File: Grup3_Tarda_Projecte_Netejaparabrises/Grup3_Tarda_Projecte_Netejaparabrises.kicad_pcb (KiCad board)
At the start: 2 copper layers, 0 parts

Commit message: Layout 3
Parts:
- added C1: 100n, Capacitor_SMD:C_0805_2012Metric, F.Cu at (38.5, 68.0)
- added C2: 0.33u, Capacitor_THT:C_Disc_D3.0mm_W1.6mm_P2.50mm, F.Cu at (37.8, 65.2)
- added C3: 0.1u, Capacitor_THT:C_Disc_D3.0mm_W1.6mm_P2.50mm, F.Cu at (37.8, 44.6)
- added C4: 100n, Capacitor_SMD:C_0805_2012Metric, F.Cu at (38.5, 42.1)
- added CClock1: 22p, Capacitor_SMD:C_0805_2012Metric, F.Cu at (105.3, 61.2)
- added CClock2: 22p, Capacitor_SMD:C_0805_2012Metric, F.Cu at (105.3, 73.4)
- added CDesOpam1: 100n, Capacitor_SMD:C_0805_2012Metric, F.Cu at (77.0, 67.2)
- added CDesacobCan1: 100n, Capacitor_SMD:C_0805_2012Metric, F.Cu at (138.8, 72.6)
- added CDesacobMicro1: 100n, Capacitor_SMD:C_0805_2012Metric, F.Cu at (122.6, 66.7)
- added D1: 1N4002, Diode_THT:D_DO-41_SOD81_P10.16mm_Horizontal, F.Cu at (38.4, 75.6)
- added D10: 1N5400, Diode_THT:D_DO-201AD_P15.24mm_Horizontal, F.Cu at (161.8, 91.9)
- added D11: 1N5400, Diode_THT:D_DO-201AD_P15.24mm_Horizontal, F.Cu at (193.3, 92.0)
- added D12: 1N5400, Diode_THT:D_DO-201AD_P15.24mm_Horizontal, F.Cu at (221.2, 118.0)
- added D2: 35V, Diode_THT:D_5W_P5.08mm_Vertical_AnodeUp, F.Cu at (38.9, 71.8)
- added D3: LED, LED_SMD:LED_0805_2012Metric_Pad1.15x1.40mm_HandSolder, F.Cu at (38.7, 49.7)
- added D4: 1N5400, Diode_THT:D_DO-201AD_P15.24mm_Horizontal, F.Cu at (221.2, 87.4)
- added D5: 1N5400, Diode_THT:D_DO-201AD_P15.24mm_Horizontal, F.Cu at (43.3, 92.2)
- added D6: 1N5400, Diode_THT:D_DO-201AD_P15.24mm_Horizontal, F.Cu at (102.2, 91.8)
- added D7: 1N5400, Diode_THT:D_DO-201AD_P15.24mm_Horizontal, F.Cu at (72.3, 92.0)
- added D8: 1N5400, Diode_THT:D_DO-201AD_P15.24mm_Horizontal, F.Cu at (221.2, 46.5)
- added D9: 1N5400, Diode_THT:D_DO-201AD_P15.24mm_Horizontal, F.Cu at (131.8, 92.1)
- added FL1: BLM03HD331SZ1D, BLM03HD331SZ1D:BEADC0603X33N, F.Cu at (47.8, 57.3)
- added FL2: BLM03HD331SZ1D, BLM03HD331SZ1D:BEADC0603X33N, F.Cu at (86.0, 83.0)
- added FL3: BLM03HD331SZ1D, BLM03HD331SZ1D:BEADC0603X33N, F.Cu at (162.0, 83.0)
- added FL4: BLM03HD331SZ1D, BLM03HD331SZ1D:BEADC0603X33N, F.Cu at (213.2, 73.1)
- added IC1: L78S05CV, L78S05CV:TO-220-STANDING, F.Cu at (39.8, 57.3)
- added IC2: PIC18F258-I_SO, Package_SO:SOIC-28W_7.5x17.9mm_P1.27mm, F.Cu at (114.8, 64.8)
- added J1: Screw_Terminal_01x02, Connector_PinSocket_2.54mm:PinSocket_1x02_P2.54mm_Vertical, F.Cu at (34.1, 91.0)
- added J2: BOTONERA, Connector_PinSocket_2.54mm:PinSocket_1x06_P2.54mm_Vertical, F.Cu at (102.5, 31.3)
- added J3: PROGRAMMING CON, Connector_PinSocket_2.54mm:PinSocket_1x05_P2.54mm_Vertical, F.Cu at (143.5, 52.2)
- added J4: JP1, Connector_PinSocket_2.54mm:PinSocket_1x03_P2.54mm_Vertical, F.Cu at (131.4, 56.5)
- added J5: DE9_Plug_MountingHoles, Connector_Dsub:DSUB-9_Female_Horizontal_P2.77x2.84mm_EdgePinOffset4.94mm_Housed_MountingHolesOffset7.48mm, F.Cu at (158.9, 43.7)
- added J6: DE9_Plug_MountingHoles, Connector_Dsub:DSUB-9_Female_Horizontal_P2.77x2.84mm_EdgePinOffset4.94mm_Housed_MountingHolesOffset7.48mm, F.Cu at (191.5, 43.7)
- added J7: CONEXIOSENSOR, Connector_PinSocket_2.54mm:PinSocket_1x02_P2.54mm_Vertical, F.Cu at (68.0, 54.6)
- added J8: CONNECTOR ALIMENTACIO 01x10, Connector_PinSocket_2.54mm:PinSocket_1x10_P2.54mm_Vertical, F.Cu at (184.9, 124.8)
- added K1: 1393280-6, V23076A1001C133:V23076A1001C133, F.Cu at (233.9, 87.4)
- added K2: 1393280-6, V23076A1001C133:V23076A1001C133, F.Cu at (34.4, 104.6)
- added K3: 1393280-6, V23076A1001C133:V23076A1001C133, F.Cu at (93.2, 104.6)
- added K4: 1393280-6, V23076A1001C133:V23076A1001C133, F.Cu at (63.3, 104.7)
- added K5: 1393280-6, V23076A1001C133:V23076A1001C133, F.Cu at (234.1, 55.3)
- added K6: 1393280-6, V23076A1001C133:V23076A1001C133, F.Cu at (122.9, 104.7)
- added K7: 1393280-6, V23076A1001C133:V23076A1001C133, F.Cu at (152.8, 104.7)
- added K8: 1393280-6, V23076A1001C133:V23076A1001C133, F.Cu at (184.2, 104.6)
- added K9: 1393280-6, V23076A1001C133:V23076A1001C133, F.Cu at (233.8, 117.9)
- added Q1: BC817-25_RF, BC817-25_RF:SOT95P237X112-3N, F.Cu at (219.9, 67.2)
- added Q2: BC817-25_RF, BC817-25_RF:SOT95P237X112-3N, F.Cu at (127.8, 92.9)
- added Q3: BC817-25_RF, BC817-25_RF:SOT95P237X112-3N, F.Cu at (98.2, 92.7)
- added Q4: BC817-25_RF, BC817-25_RF:SOT95P237X112-3N, F.Cu at (219.6, 52.0)
- added Q5: BC817-25_RF, BC817-25_RF:SOT95P237X112-3N, F.Cu at (157.8, 92.8)
- added Q6: BC817-25_RF, BC817-25_RF:SOT95P237X112-3N, F.Cu at (189.2, 92.9)
- added Q7: BC817-25_RF, BC817-25_RF:SOT95P237X112-3N, F.Cu at (222.2, 93.5)
- added R1: 220, Resistor_SMD:R_0805_2012Metric_Pad1.20x1.40mm_HandSolder, F.Cu at (38.6, 47.1)
- added R10: 13.4R, Resistor_SMD:R_0805_2012Metric_Pad1.20x1.40mm_HandSolder, F.Cu at (95.2, 92.6)
- added R11: 620.3R, Resistor_SMD:R_0805_2012Metric_Pad1.20x1.40mm_HandSolder, F.Cu at (216.4, 57.0)
- added R12: 319.6R, Resistor_SMD:R_0805_2012Metric_Pad1.20x1.40mm_HandSolder, F.Cu at (219.3, 57.0)
- added R13: 13.4R, Resistor_SMD:R_0805_2012Metric_Pad1.20x1.40mm_HandSolder, F.Cu at (222.3, 57.0)
- added R14: 620.3R, Resistor_SMD:R_0805_2012Metric_Pad1.20x1.40mm_HandSolder, F.Cu at (155.6, 87.5)
- added R15: 620.3R, Resistor_SMD:R_0805_2012Metric_Pad1.20x1.40mm_HandSolder, F.Cu at (186.9, 87.5)
- added R16: 319.6R, Resistor_SMD:R_0805_2012Metric_Pad1.20x1.40mm_HandSolder, F.Cu at (155.6, 89.6)
- added R17: 319.6R, Resistor_SMD:R_0805_2012Metric_Pad1.20x1.40mm_HandSolder, F.Cu at (186.9, 89.8)
- added R18: 13.4R, Resistor_SMD:R_0805_2012Metric_Pad1.20x1.40mm_HandSolder, F.Cu at (154.7, 92.9)
- added R19: 13.4R, Resistor_SMD:R_0805_2012Metric_Pad1.20x1.40mm_HandSolder, F.Cu at (186.1, 93.0)
- added R2: 620.3R, Resistor_SMD:R_0805_2012Metric_Pad1.20x1.40mm_HandSolder, F.Cu at (216.9, 62.7)
- added R20: 620.3R, Resistor_SMD:R_0805_2012Metric_Pad1.20x1.40mm_HandSolder, F.Cu at (216.4, 96.0)
- added R21: 319.6R, Resistor_SMD:R_0805_2012Metric_Pad1.20x1.40mm_HandSolder, F.Cu at (218.8, 96.0)
- added R22: 13.4R, Resistor_SMD:R_0805_2012Metric_Pad1.20x1.40mm_HandSolder, F.Cu at (222.1, 96.9)
- added R3: 620.3R, Resistor_SMD:R_0805_2012Metric_Pad1.20x1.40mm_HandSolder, F.Cu at (125.4, 87.3)
- added R4: 620.3R, Resistor_SMD:R_0805_2012Metric_Pad1.20x1.40mm_HandSolder, F.Cu at (96.2, 87.2)
- added R5: 319.6R, Resistor_SMD:R_0805_2012Metric_Pad1.20x1.40mm_HandSolder, F.Cu at (220.1, 62.7)
- added R6: 319.6R, Resistor_SMD:R_0805_2012Metric_Pad1.20x1.40mm_HandSolder, F.Cu at (125.5, 89.7)
- added R7: 319.6R, Resistor_SMD:R_0805_2012Metric_Pad1.20x1.40mm_HandSolder, F.Cu at (96.2, 89.5)
- added R8: 13.4R, Resistor_SMD:R_0805_2012Metric_Pad1.20x1.40mm_HandSolder, F.Cu at (223.1, 62.7)
- added R9: 13.4R, Resistor_SMD:R_0805_2012Metric_Pad1.20x1.40mm_HandSolder, F.Cu at (124.7, 92.9)
- added RBot1: 22k, Resistor_SMD:R_0805_2012Metric_Pad1.20x1.40mm_HandSolder, F.Cu at (102.9, 50.4)
- added RBot2: 22k, Resistor_SMD:R_0805_2012Metric_Pad1.20x1.40mm_HandSolder, F.Cu at (105.7, 50.4)
- added RBot3: 22k, Resistor_SMD:R_0805_2012Metric_Pad1.20x1.40mm_HandSolder, F.Cu at (109.0, 50.4)
- added RBot4: 22k, Resistor_SMD:R_0805_2012Metric_Pad1.20x1.40mm_HandSolder, F.Cu at (112.4, 50.4)
- added RPOT1: 10k, POTENCIOMETRE:TRIM_3362P-1-103, F.Cu at (68.5, 61.4)
- added RReset1: 4.7k, Resistor_SMD:R_0805_2012Metric_Pad1.20x1.40mm_HandSolder, F.Cu at (134.2, 60.0)
- added RSens1: 1k, Resistor_SMD:R_0805_2012Metric_Pad1.20x1.40mm_HandSolder, F.Cu at (74.5, 56.6)
- added Rterm1: 120R, Resistor_SMD:R_0805_2012Metric_Pad1.20x1.40mm_HandSolder, F.Cu at (149.3, 71.8)
- added SW1: SW_SPST, Library:AS11CH, F.Cu at (109.0, 40.3)
- added SW2: SW_SP3T, SW_NR01103ANG13-1C:SW_NR01103ANG13-1C, F.Cu at (120.6, 41.7)
- added SWReset1: SW_Push, Button_Switch_SMD:SW_Push_SPST_NO_Alps_SKRK, F.Cu at (136.0, 56.4)
- added U1: Value, Package_SO:SOIC-8_3.9x4.9mm_P1.27mm, F.Cu at (144.3, 71.8)
- added U2: LM393, Package_SO:SOIC-8_3.9x4.9mm_P1.27mm, F.Cu at (75.3, 61.5)
- added Y1: ABLS2-8.000MHZ-D4Y-T, XTAL_ABLS2-8:XTAL_ABLS2-8.000MHZ-D4Y-T, F.Cu at (101.5, 67.3)
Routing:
- net DriverM2: track 0.00 -> 149.6 mm
- net VMOT1-: track 0.00 -> 123.8 mm
- net VBOMBA2: track 0.00 -> 110.4 mm
- net DriverB1: track 0.00 -> 99.0 mm, vias 0 -> 2
- net VMOT1+: track 0.00 -> 90.5 mm
- net VBOMBA1: track 0.00 -> 75.8 mm
- net /Digital/Tx: track 0.00 -> 68.8 mm
- net /Digital/Rx: track 0.00 -> 66.8 mm
- net EN2: track 0.00 -> 66.7 mm
- net EN1: track 0.00 -> 65.4 mm
- net /Potencia/Vc_m2: track 0.00 -> 62.8 mm
- net /Digital/CANH: track 0.00 -> 61.8 mm
- net /Potencia/Vc_m1: track 0.00 -> 61.4 mm
- net /Digital/CANL: track 0.00 -> 59.7 mm
- net VLUNETA: track 0.00 -> 45.4 mm
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- added copper zone on In1.Cu, net +VCC
- added copper zone on F.Cu, net GND
- added copper zone on In2.Cu, net GND
- added copper zone on In2.Cu, net GNDPWR
- added copper zone on In1.Cu, net VBAT
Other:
- board outline added: 254.4 x 101.6 mm
- copper layers 2 -> 4

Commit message: canvis divisor sensor de pluja, node vbat protegit, connector de motors, README
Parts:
- moved FL2 125.6 mm to (148.0, -26.3)
- moved K9 118.2 mm to (118.0, 141.6), turned to 0 degrees
- moved FL3 116.8 mm to (190.8, -30.1)
- moved D12 103.9 mm to (117.8, 129.1), turned to 0 degrees
- moved FL4 103.7 mm to (228.5, -29.4)
- moved FL1 103.5 mm to (113.8, -22.5)
- moved K5 101.9 mm to (180.6, 142.0), turned to 0 degrees
- moved K1 101.2 mm to (148.5, 141.8), turned to 0 degrees
- moved R22 89.5 mm to (139.0, 130.0), turned to 90 degrees
- moved J8 88.9 mm to (258.0, 74.1), turned to 0 degrees
- moved D8 88.6 mm to (189.4, 129.1), turned to 0 degrees
- moved Q7 87.7 mm to (142.4, 130.0), turned to -90 degrees
- moved R13 85.1 mm to (178.9, 130.2), turned to 0 degrees
- moved R21 84.6 mm to (139.9, 126.7), turned to 0 degrees
- moved R8 84.6 mm to (173.2, 131.0), turned to 0 degrees
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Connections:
- C1 pad 1: /Alimentacio/V_{in} -> VBAT
- C2 pad 1: /Alimentacio/V_{in} -> VBAT
- C3 pad 2: GNDPWR -> GND
- C4 pad 2: GNDPWR -> GND
- D1 pad 1: /Alimentacio/V_{in} -> VBAT
- D1 pad 2: VBAT -> /Alimentacio/Vbat
- D2 pad 1: /Alimentacio/V_{in} -> VBAT
- IC1 pad 1: /Alimentacio/V_{in} -> VBAT
- J1 pad 1: VBAT -> /Alimentacio/Vbat
- R1 pad 2: GNDPWR -> GND
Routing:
- net DriverM2: track 149.6 -> 0.00 mm
- net VMOT1-: track 123.8 -> 0.00 mm
- net VBOMBA2: track 110.4 -> 0.00 mm
- net DriverB1: track 99.0 -> 0.00 mm, vias 2 -> 0
- net VMOT1+: track 90.5 -> 0.00 mm
- net VBOMBA1: track 75.8 -> 0.00 mm
- net /Digital/Tx: track 68.8 -> 0.00 mm
- net /Digital/Rx: track 66.8 -> 0.00 mm
- net EN2: track 66.7 -> 0.00 mm
- net EN1: track 65.4 -> 0.00 mm
- net /Potencia/Vc_m2: track 62.8 -> 0.00 mm
- net /Digital/CANH: track 61.8 -> 0.00 mm
- net /Potencia/Vc_m1: track 61.4 -> 0.00 mm
- net /Digital/CANL: track 59.7 -> 0.00 mm
- net VLUNETA: track 45.4 -> 0.00 mm
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- removed copper zone on In1.Cu, net +VCC
- removed copper zone on In2.Cu, net GND
- removed copper zone on In2.Cu, net GNDPWR
- removed copper zone on In1.Cu, net VBAT
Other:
- board outline removed

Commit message: placement
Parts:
- added J10: Screw_Terminal_01x02, TerminalBlock_Phoenix:TerminalBlock_Phoenix_MKDS-1,5-2-5.08_1x02_P5.08mm_Horizontal, F.Cu at (26.2, 109.0)
- added J11: Screw_Terminal_01x02, TerminalBlock_Phoenix:TerminalBlock_Phoenix_MKDS-1,5-2-5.08_1x02_P5.08mm_Horizontal, F.Cu at (169.8, 114.7)
- added J12: Screw_Terminal_01x02, TerminalBlock_Phoenix:TerminalBlock_Phoenix_MKDS-1,5-2-5.08_1x02_P5.08mm_Horizontal, F.Cu at (156.0, 169.2)
- added J9: Screw_Terminal_01x02, TerminalBlock_Phoenix:TerminalBlock_Phoenix_MKDS-1,5-2-5.08_1x02_P5.08mm_Horizontal, F.Cu at (112.0, 169.1)
- added R23: 10k, Resistor_SMD:R_0805_2012Metric_Pad1.20x1.40mm_HandSolder, F.Cu at (53.5, 67.7)
- J1: footprint Connector_PinSocket_2.54mm:PinSocket_1x02_P2.54mm_Vertical -> TerminalBlock_Phoenix:TerminalBlock_Phoenix_MKDS-1,5-2-5.08_1x02_P5.08mm_Horizontal
- J8: value CONNECTOR ALIMENTACIO 01x10 -> Screw_Terminal_01x02; footprint Connector_PinSocket_2.54mm:PinSocket_1x10_P2.54mm_Vertical -> TerminalBlock_Phoenix:TerminalBlock_Phoenix_MKDS-1,5-2-5.08_1x02_P5.08mm_Horizontal
- moved J8 228.6 mm to (49.9, 168.7)
- moved R8 142.8 mm to (34.5, 96.5), turned to 90 degrees
- moved R5 141.9 mm to (35.5, 93.5)
- moved R2 141.6 mm to (35.5, 91.5), turned to 0 degrees
- moved Q1 135.0 mm to (37.4, 96.5), turned to -90 degrees
- moved K1 118.4 mm to (35.0, 108.0)
- moved D4 96.2 mm to (58.2, 95.7), turned to 180 degrees
- moved J5 85.9 mm to (74.1, 57.7)
- moved FL1 79.3 mm to (160.7, 41.5)
- moved Q6 78.5 mm to (122.6, 134.7)
- moved R19 78.5 mm to (119.5, 134.7)
- moved D11 78.5 mm to (126.7, 133.8)
- moved K8 78.5 mm to (117.7, 146.3)
- moved R15 78.5 mm to (120.4, 129.2)
- moved R17 78.5 mm to (120.4, 131.5)
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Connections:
- J8 pad 1: VMOT1+ -> VMOT1-
- J8 pad 2: VMOT1- -> VMOT1+
- RPOT1 pad 1: +VCC -> /Analog/Vsensibilitat
- RPOT1 pad 2: /Analog/Vsensibilitat -> GND
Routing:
- removed copper zone on F.Cu, net GND
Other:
- board outline added: 159.2 x 126.4 mm

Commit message: powersilkscreen
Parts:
- moved J8 6.83 mm to (43.0, 168.9)
- moved RBot1 5.30 mm to (144.4, 83.3)
- moved RBot2 5.30 mm to (144.4, 80.5)
- moved RBot3 5.30 mm to (144.4, 77.2)
- moved RBot4 5.30 mm to (144.4, 73.8)
- moved SW1 5.30 mm to (154.3, 72.3)
- moved SW2 5.30 mm to (166.7, 72.2)
- moved R20 5.19 mm to (174.3, 129.3)
- moved Q7 5.18 mm to (176.8, 135.0)
- moved R21 5.18 mm to (174.3, 131.6)
- moved R22 5.18 mm to (173.4, 135.0)
- moved J12 5.01 mm to (151.0, 168.8)
- moved CDesOpam1 4.86 mm to (52.9, 67.0)
- moved J7 4.86 mm to (43.8, 51.6)
- moved R23 4.86 mm to (48.6, 67.7)
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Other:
- board size 159.2 x 126.4 mm -> 162.4 x 126.4 mm

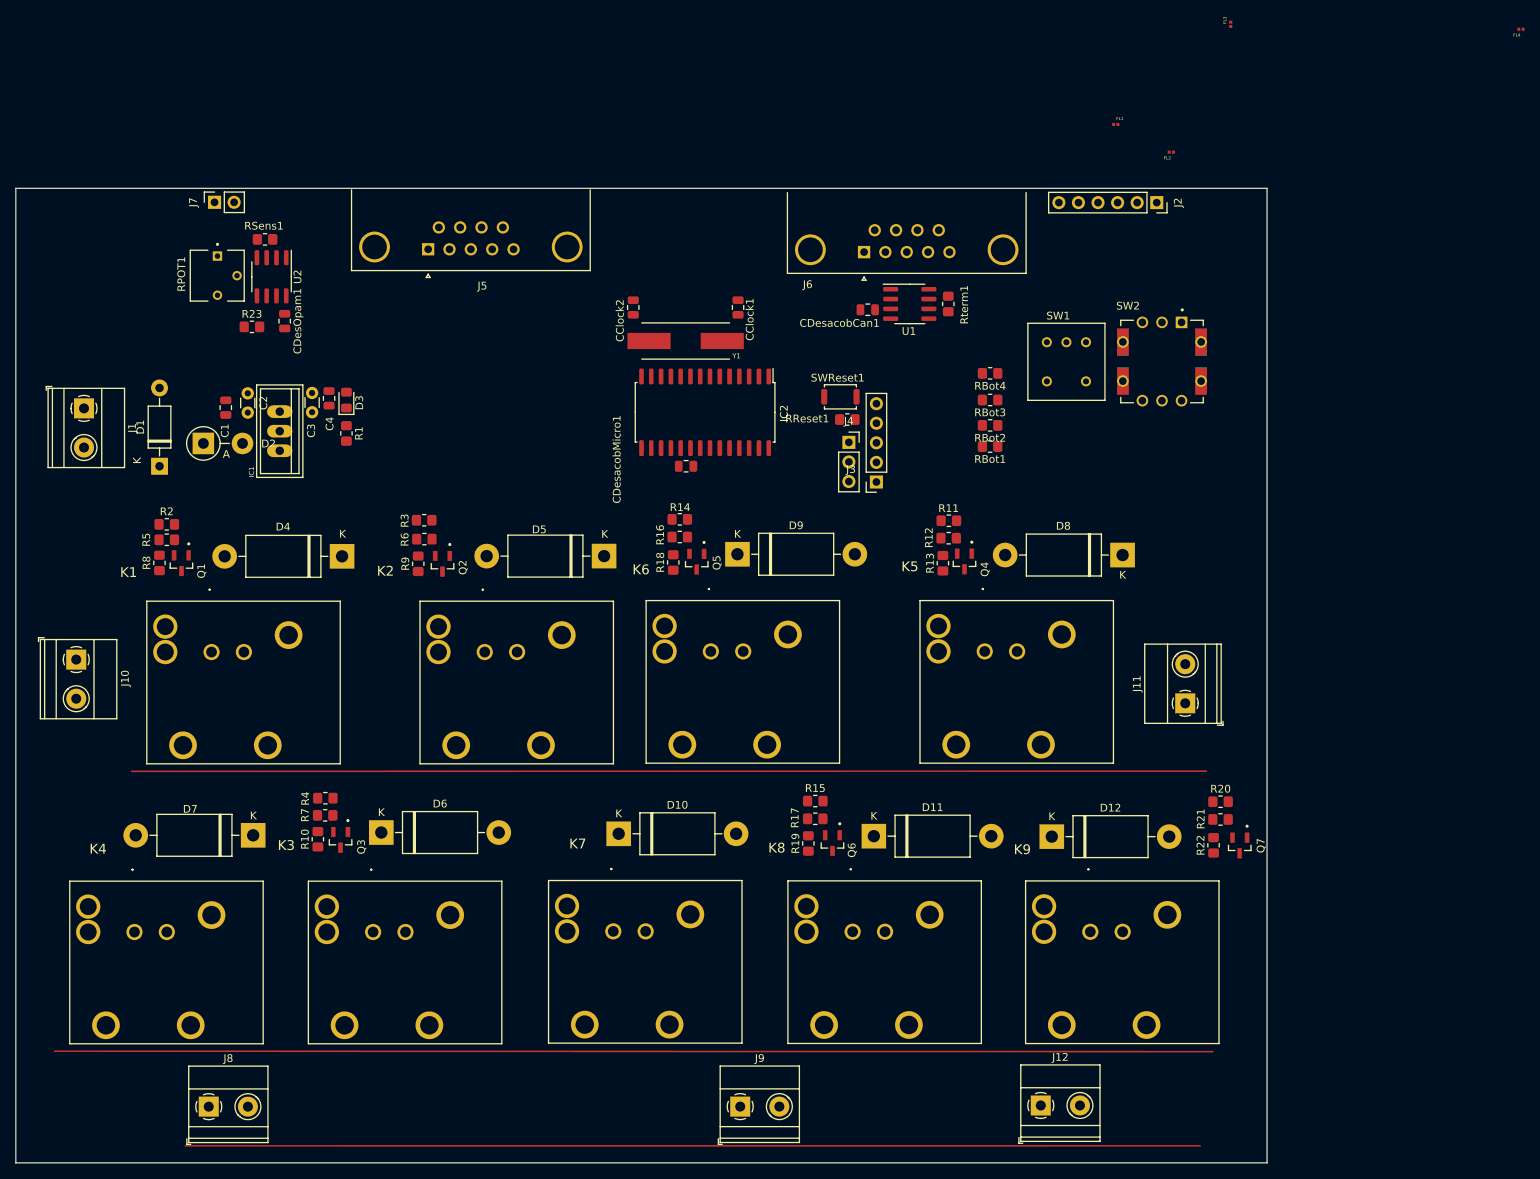
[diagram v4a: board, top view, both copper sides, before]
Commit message: plans de massa i alimentacio layout
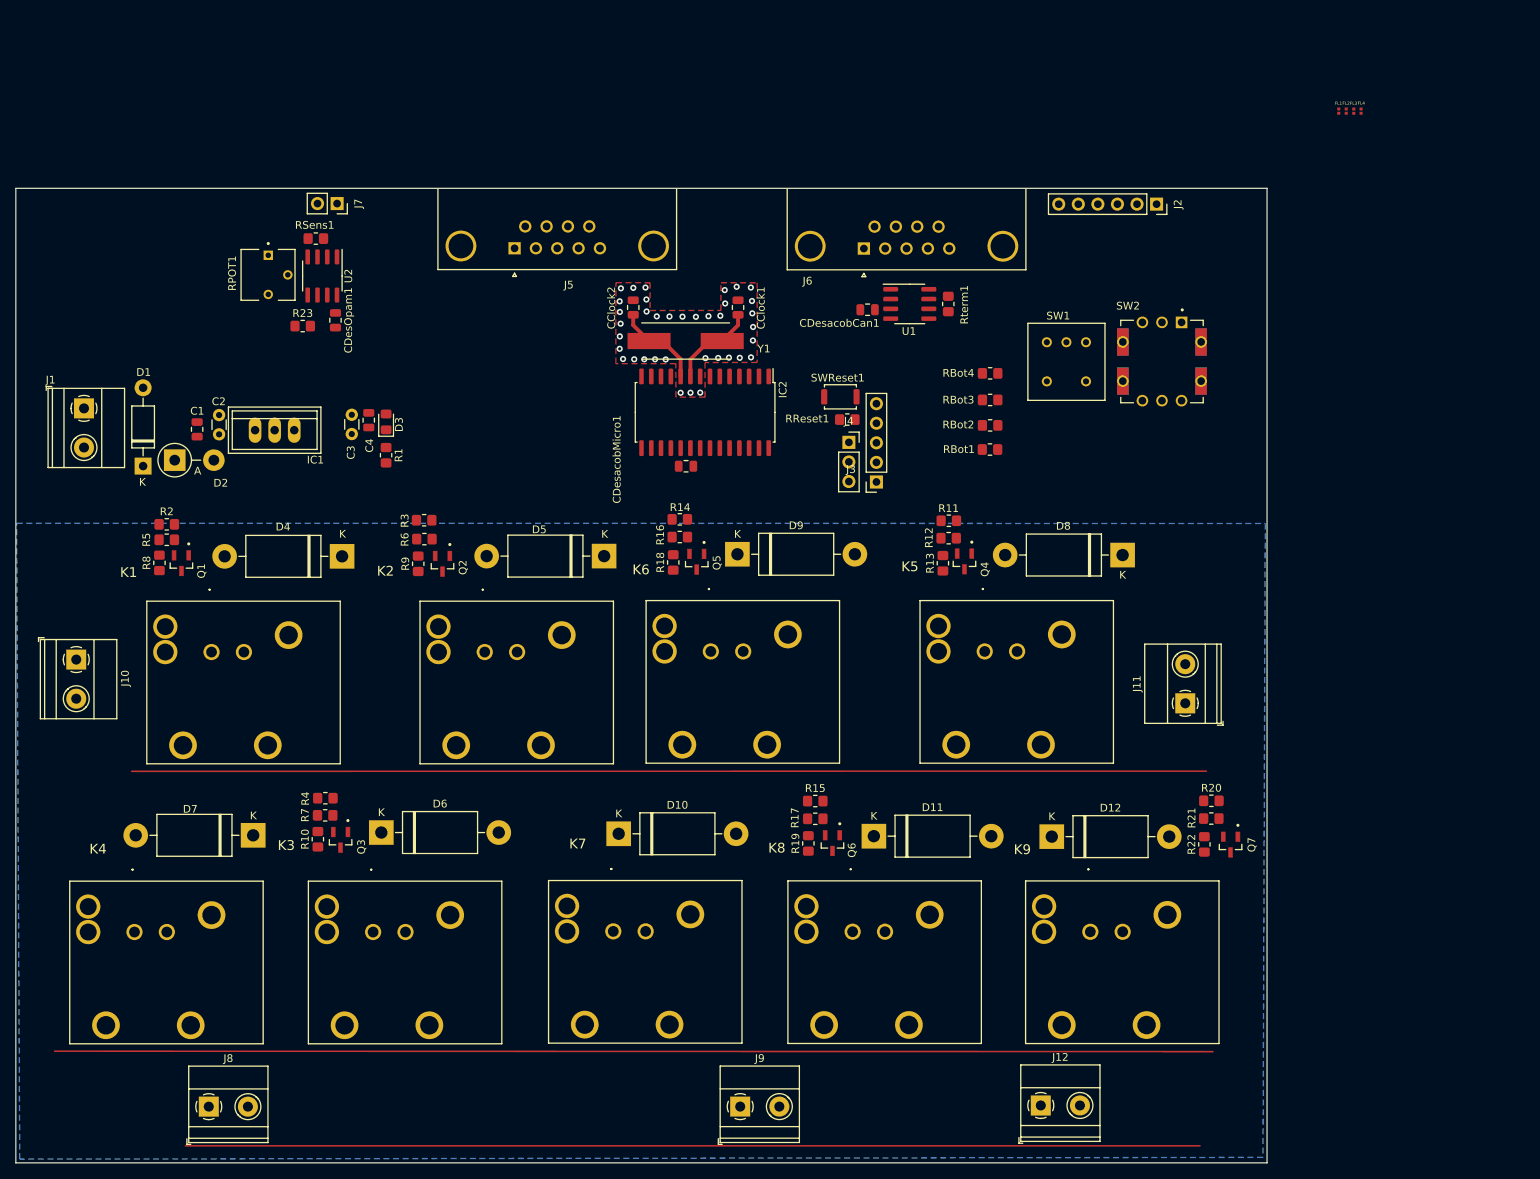
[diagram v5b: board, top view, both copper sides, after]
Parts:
- moved FL1 29.0 mm to (189.7, 39.7), turned to 90 degrees
- moved FL2 23.3 mm to (190.6, 39.7), turned to 90 degrees
- moved FL4 23.3 mm to (192.6, 39.7), turned to 90 degrees
- moved FL3 19.5 mm to (191.6, 39.7)
- moved J7 15.9 mm to (59.7, 51.7), turned to -90 degrees
- moved J5 11.2 mm to (82.7, 57.5)
- moved U2 6.59 mm to (57.8, 61.1)
- moved CDesOpam1 6.59 mm to (59.5, 66.9)
- moved R23 6.59 mm to (55.2, 67.6)
- moved RPOT1 6.59 mm to (50.8, 61.0)
- moved RSens1 6.59 mm to (56.9, 56.3)
- moved D3 5.88 mm to (66.0, 80.1)
- moved C3 5.88 mm to (61.6, 79.1)
- moved C4 5.88 mm to (63.8, 79.8)
- moved R1 5.88 mm to (66.0, 84.4)
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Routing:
- net /Digital/XTAL1: track 0.00 -> 11.6 mm
- net /Digital/XTAL2: track 0.00 -> 11.6 mm
- net GND: vias 0 -> 37
- added copper zone on In1.Cu, net +VCC
- added copper zone on F.Cu, net GND
- added copper zone on In2.Cu, net GND
- added copper zone on B.Cu, net GNDPWR
- added copper zone on In2.Cu, net GNDPWR
- added copper zone on In1.Cu, net VBAT

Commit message: routing v1 sense acabar
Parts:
- removed D2: 35V, Diode_THT:D_5W_P5.08mm_Vertical_AnodeUp
- removed FL1, FL2, FL3, FL4: BLM03HD331SZ1D, BLM03HD331SZ1D:BEADC0603X33N
- removed SW1: SW_SPST, Library:AS11CH
- removed SW2: SW_SP3T, SW_NR01103ANG13-1C:SW_NR01103ANG13-1C
- added REF96: MountingHole_3.2mm_M3_ISO7380, MountingHole:MountingHole_3.2mm_M3_ISO7380, F.Cu at (220.0, 36.8)
- added REF97: MountingHole_3.2mm_M3_ISO7380, MountingHole:MountingHole_3.2mm_M3_ISO7380, F.Cu at (219.8, 155.1)
- added REF98: MountingHole_3.2mm_M3_ISO7380, MountingHole:MountingHole_3.2mm_M3_ISO7380, F.Cu at (65.8, 155.1)
- added REF99: MountingHole_3.2mm_M3_ISO7380, MountingHole:MountingHole_3.2mm_M3_ISO7380, F.Cu at (65.6, 36.7)
- C1, C4, CClock1, CClock2, CDesOpam1, CDesacobCan1, CDesacobMicro1: footprint Capacitor_SMD:C_0805_2012Metric -> Capacitor_THT:C_Disc_D3.0mm_W1.6mm_P2.50mm
- moved D8 51.0 mm to (209.7, 80.3)
- moved D1 49.1 mm to (80.6, 68.8)
- moved Q7 48.8 mm to (221.4, 117.9)
- moved Q4 48.3 mm to (186.3, 81.2)
- moved D3 48.2 mm to (111.2, 63.1)
- moved R1 48.2 mm to (111.2, 67.4)
- moved Q2 48.2 mm to (118.5, 81.5)
- moved Q6 48.0 mm to (168.8, 117.5)
- moved R20 47.7 mm to (216.8, 109.9)
- moved R2 47.6 mm to (81.2, 74.3)
- moved R4 47.6 mm to (101.8, 109.8)
- moved Q5 47.6 mm to (150.8, 81.2)
- moved Q3 47.6 mm to (104.6, 117.3)
- moved R15 47.6 mm to (165.4, 110.4)
- moved D5 47.5 mm to (138.7, 80.5)
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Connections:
- net /Digital/CANH renamed /Digital/CAN-
- net /Digital/CANL renamed /Digital/CAN+
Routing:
- net Sensordig_o: track 0.00 -> 74.6 mm
- net DriverB1: track 0.00 -> 74.1 mm
- net /Potencia/Vc_m2: track 0.00 -> 71.2 mm
- net EN1: track 0.00 -> 66.3 mm
- net EN2: track 0.00 -> 66.2 mm
- net /Potencia/Vc_m1: track 0.00 -> 47.6 mm
- net /Digital/Vboto1: track 0.00 -> 44.1 mm
- net EnableM1: track 0.00 -> 43.4 mm, vias 0 -> 2
- net GNDPWR: track 0.00 -> 39.9 mm, vias 0 -> 14
- net /Digital/Tx: track 0.00 -> 38.5 mm
- net /Digital/Vboto2: track 0.00 -> 38.1 mm
- net PGC: track 0.00 -> 34.2 mm
- net VBOMBA2: track 0.00 -> 34.0 mm
- net /Digital/Vboto3: track 0.00 -> 33.7 mm
- net /Potencia/Vc_lu: track 0.00 -> 33.6 mm
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- removed copper zone on B.Cu, net GNDPWR
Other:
- board size 162.4 x 126.4 mm -> 162.4 x 126.5 mm

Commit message: Routing
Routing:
- net DriverLuneta: track 0.00 -> 92.6 mm, vias 0 -> 2
- net DriverM1: track 0.00 -> 76.3 mm, vias 0 -> 2
- net DriverM2: track 0.00 -> 51.9 mm, vias 0 -> 2
- net /Potencia/Vc_m1: track 47.6 -> 99.0 mm
- net /Digital/Vboto1: track 44.1 -> 94.5 mm, vias 0 -> 2
- net /Digital/Vboto4: track 27.1 -> 65.8 mm, vias 0 -> 2
- net /Digital/Vboto3: track 33.7 -> 70.1 mm, vias 0 -> 2
- net /Digital/Vboto2: track 38.1 -> 74.0 mm, vias 0 -> 3
- net DriverB2: track 0.00 -> 34.5 mm
- net /Digital/MCLR: track 0.00 -> 30.2 mm, vias 0 -> 1
- net unconnected-(J6-PAD-Pad0): track 0.00 -> 29.6 mm
- net unconnected-(J5-PAD-Pad0): track 0.00 -> 28.0 mm
- net /Digital/CANRX: track 0.00 -> 25.7 mm
- net /Digital/CANTX: track 0.00 -> 20.6 mm
- net /Potencia/Vc_EN1: track 5.85 -> 19.7 mm
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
